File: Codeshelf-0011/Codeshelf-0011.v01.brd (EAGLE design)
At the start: 35 x 30 mm, 8 parts, among them SW1 A1202UA, U1 V_REG_LDOSMD, U2 MIC94061C6

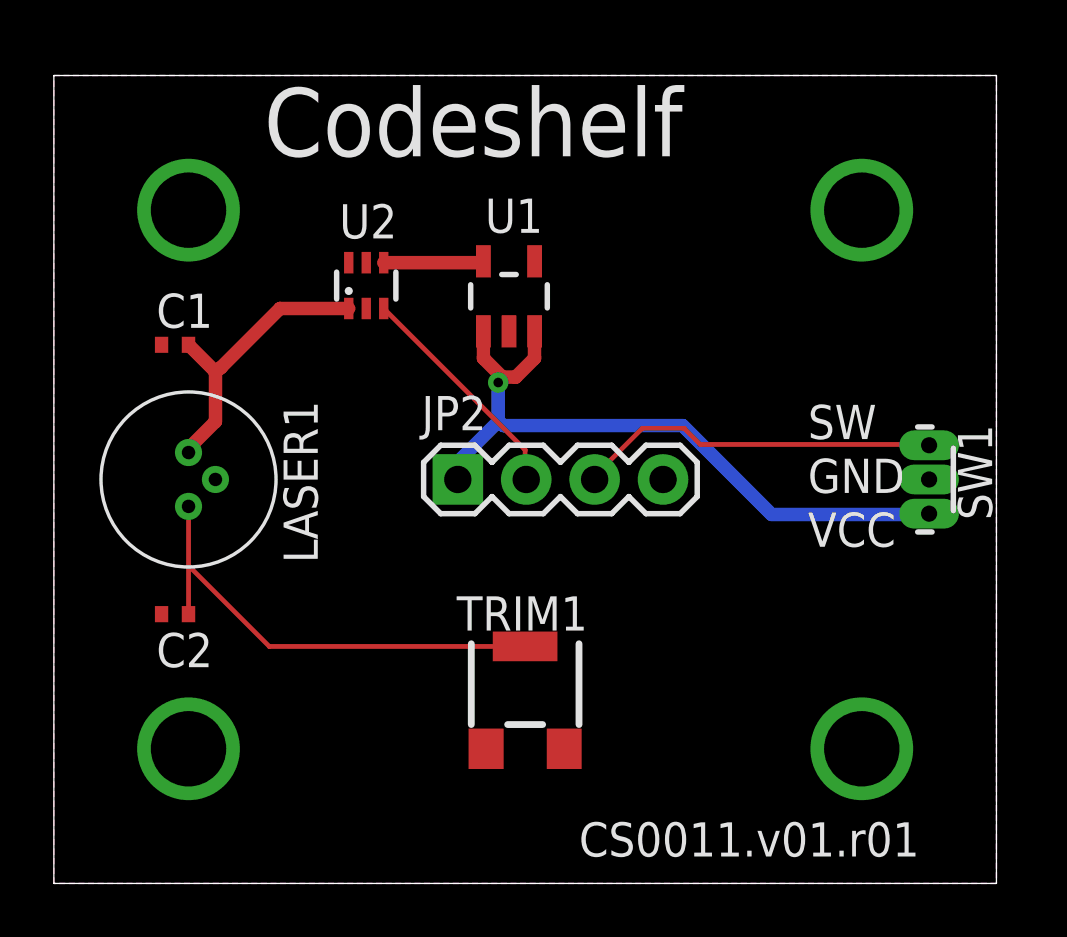
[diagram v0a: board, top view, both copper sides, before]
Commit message: cleanup repo
Cleaned up repo.
Cleaned up GW-devices.lbr
Add CS0012 - gateway dongle
CS0011 board changed to match laser from Laser66.
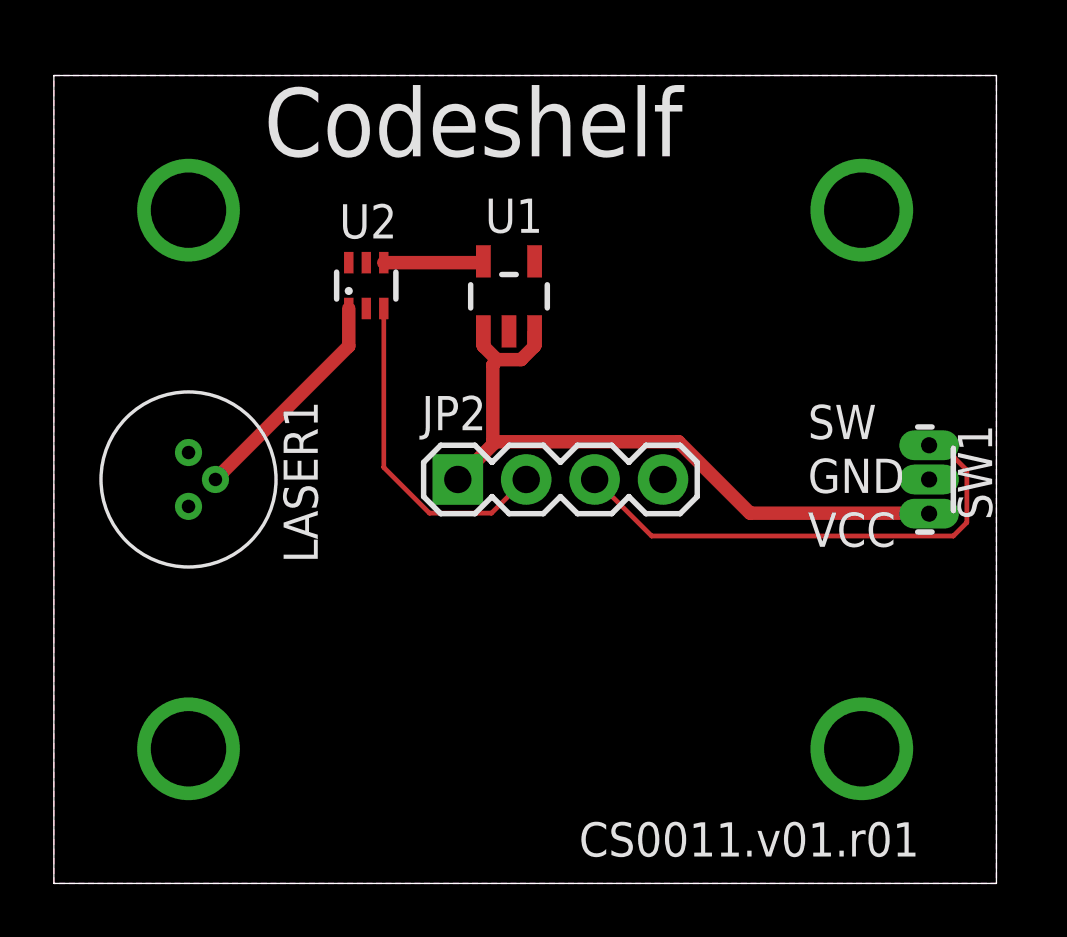
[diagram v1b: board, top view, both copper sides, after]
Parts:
- removed C1, C2: 0.1uF, GW-devices:C0402
- removed TRIM1: R-TRIM3364, GW-devices:RTRIM3364
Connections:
- removed net N$1: C1.1, LASER1.1, U2.1
- removed net N$4: C2.1, LASER1.3, TRIM1.2
- new net VCC: LASER1.2, U2.1
- net GND: now also LASER1.1; no longer C1.2, C2.2, LASER1.2, TRIM1.3
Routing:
- net N$4: track 17.7 -> 0.00 mm
- net N$1: track 10.7 -> 0.00 mm
- net VCC: track 0.00 -> 8.40 mm
- net N$3: track 13.6 -> 18.6 mm
- net N$2: track 8.56 -> 12.4 mm
- net +3V3: track 26.4 -> 25.8 mm, vias 1 -> 0
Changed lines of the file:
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@@
 <attribute name="NAME" x="16.011" y="24.159" size="1.27" layer="25"/>
 <attribute name="MFGN" value="Diodes Ince" x="16.9" y="21.8" size="1.778" layer="27" display="off"/>
-<attribute name="MFGP" value="AP7331-30WG-7" x="16.9" y="21.8" size="1.778" layer="27" display="off"/>
+<attribute name="MFGP" value="AP7331-28WG-7" x="16.9" y="21.8" size="1.778" layer="27" display="off"/>
 <attribute name="PRICE" value="0.50" x="16.9" y="21.8" size="1.778" layer="27" display="off"/>
-</element>
-<element name="TRIM1" library="GW-devices" package="RTRIM3364" value="R-TRIM3364" x="17.5" y="7" smashed="yes">
-<attribute name="NAME" x="14.96" y="9.39" size="1.27" layer="25"/>
-<attribute name="MFGN" value="Bourns" x="17.5" y="7" size="1.778" layer="27" display="off"/>
-<attribute name="MFGP" value="3364X-1-503E" x="17.5" y="7" size="1.778" layer="27" display="off"/>
-<attribute name="PRICE" value="1.00" x="17.5" y="7" size="1.778" layer="27" display="off"/>
-</element>
-<element name="C1" library="GW-devices" package="C0402" value="0.1uF" x="4.5" y="20" smashed="yes" rot="R180">
-<attribute name="NAME" x="5.9" y="21.9" size="1.27" layer="25" rot="R180"/>
-<attribute name="MFGN" value="Murata" x="4.5" y="20" size="1.778" layer="27" rot="R180" display="off"/>
-<attribute name="MFGP" value="GRM155R71C104JA88D" x="4.5" y="20" size="1.778" layer="27" rot="R180" display="off"/>
-<attribute name="PRICE" value="0.03" x="4.5" y="20" size="1.778" layer="27" rot="R180" display="off"/>
-</element>
-<element name="C2" library="GW-devices" package="C0402" value="0.1uF" x="4.5" y="10" smashed="yes" rot="R180">
-<attribute name="NAME" x="5.9" y="9.3" size="1.27" layer="25" rot="R180"/>
-<attribute name="MFGN" value="Murata" x="4.5" y="10" size="1.778" layer="27" rot="R180" display="off"/>
-<attribute name="MFGP" value="GRM155R71C104JA88D" x="4.5" y="10" size="1.778" layer="27" rot="R180" display="off"/>
-<attribute name="PRICE" value="0.03" x="4.5" y="10" size="1.778" layer="27" rot="R180" display="off"/>
 </element>
 </elements>
@@
 <contactref element="U2" pad="5"/>
 <contactref element="U2" pad="2"/>
-<contactref element="LASER1" pad="2"/>
 <contactref element="U1" pad="2"/>
 <contactref element="JP2" pad="4"/>
-<contactref element="TRIM1" pad="3"/>
-<contactref element="C2" pad="2"/>
-<contactref element="C1" pad="2"/>
 <polygon width="0.3048" layer="16">
 <vertex x="0" y="0"/>
@@
 <vertex x="35" y="0"/>
 </polygon>
+<contactref element="LASER1" pad="1"/>
 </signal>
 <signal name="+3V3" class="1">
@@
 <contactref element="U1" pad="3"/>
 <contactref element="JP2" pad="1"/>
-<wire x1="16.65" y1="18.8" x2="15.95" y2="19.5" width="0.5" layer="1"/>
-<wire x1="16.65" y1="18.8" x2="17.15" y2="18.8" width="0.5" layer="1"/>
-<wire x1="17.15" y1="18.8" x2="17.85" y2="19.5" width="0.5" layer="1"/>
-<wire x1="15.95" y1="19.5" x2="15.95" y2="20.4999" width="0.5" layer="1"/>
-<wire x1="17.85" y1="19.5" x2="17.85" y2="20.4999" width="0.5" layer="1"/>
-<wire x1="16.5" y1="17.15" x2="16.5" y2="18.6" width="0.5" layer="16"/>
-<wire x1="15" y1="15.65" x2="16.5" y2="17.15" width="0.5" layer="16"/>
-<wire x1="15" y1="15" x2="15" y2="15.65" width="0.5" layer="16"/>
-<wire x1="16.5" y1="18.6" x2="16.65" y2="18.8" width="0.5" layer="1"/>
-<wire x1="26.65" y1="13.7" x2="32.5" y2="13.7" width="0.5" layer="16"/>
-<wire x1="23.35" y1="17" x2="26.65" y2="13.7" width="0.5" layer="16"/>
-<wire x1="16.7" y1="17" x2="23.35" y2="17" width="0.5" layer="16"/>
-<wire x1="32.5" y1="13.7" x2="32.5" y2="13.73" width="0.5" layer="16"/>
-<wire x1="16.5" y1="17.15" x2="16.7" y2="17" width="0.5" layer="16"/>
-<via x="16.5" y="18.6" extent="1-16" drill="0.3556"/>
+<wire x1="15.95" y1="19.95" x2="15.95" y2="20.4999" width="0.5" layer="1"/>
+<wire x1="16.45" y1="19.45" x2="15.95" y2="19.95" width="0.5" layer="1"/>
+<wire x1="17.35" y1="19.45" x2="16.45" y2="19.45" width="0.5" layer="1"/>
+<wire x1="17.85" y1="19.95" x2="17.35" y2="19.45" width="0.5" layer="1"/>
+<wire x1="17.85" y1="20.4999" x2="17.85" y2="19.95" width="0.5" layer="1"/>
+<wire x1="16.3" y1="16.3" x2="16.3" y2="16.4" width="0.5" layer="1"/>
+<wire x1="16.3" y1="16.4" x2="16.3" y2="19.25" width="0.5" layer="1"/>
+<wire x1="15" y1="15" x2="16.3" y2="16.3" width="0.5" layer="1"/>
+<wire x1="16.3" y1="19.25" x2="16.45" y2="19.45" width="0.5" layer="1"/>
+<wire x1="25.85" y1="13.75" x2="32.5" y2="13.75" width="0.5" layer="1"/>
+<wire x1="23.2" y1="16.4" x2="25.85" y2="13.75" width="0.5" layer="1"/>
+<wire x1="16.3" y1="16.4" x2="23.2" y2="16.4" width="0.5" layer="1"/>
+<wire x1="32.5" y1="13.75" x2="32.5" y2="13.73" width="0.5" layer="1"/>
 </signal>
 <signal name="N$5">
@@
 <contactref element="U2" pad="4"/>
 <contactref element="U1" pad="5"/>
-<wire x1="12.25" y1="23.05" x2="15.9" y2="23.05" width="0.5" layer="1"/>
-<wire x1="15.9" y1="23.05" x2="15.95" y2="23.1001" width="0.5" layer="1"/>
-<wire x1="15.95" y1="23.1001" x2="15.95" y2="23.1" width="0.5" layer="1"/>
-</signal>
-<signal name="N$1" class="3">
-<contactref element="U2" pad="1"/>
-<contactref element="LASER1" pad="1"/>
-<contactref element="C1" pad="1"/>
-<wire x1="6" y1="19" x2="5" y2="20" width="0.5" layer="1"/>
-<wire x1="6" y1="17.15" x2="6" y2="19" width="0.5" layer="1"/>
-<wire x1="5" y1="16.15" x2="6" y2="17.15" width="0.5" layer="1"/>
-<wire x1="5" y1="16" x2="5" y2="16.15" width="0.5" layer="1"/>
-<wire x1="8.4" y1="21.35" x2="10.95" y2="21.35" width="0.5" layer="1"/>
-<wire x1="6.2" y1="19.15" x2="8.4" y2="21.35" width="0.5" layer="1"/>
-<wire x1="6" y1="19" x2="6.2" y2="19.15" width="0.5" layer="1"/>
+<wire x1="15.9" y1="23.05" x2="12.25" y2="23.05" width="0.5" layer="1"/>
+<wire x1="15.95" y1="23.1" x2="15.9" y2="23.05" width="0.5" layer="1"/>
+<wire x1="15.95" y1="23.1" x2="15.95" y2="23.1001" width="0.5" layer="1"/>
 </signal>
 <signal name="N$2">
 <contactref element="U2" pad="3"/>
 <contactref element="JP2" pad="2"/>
-<wire x1="17.5" y1="16.1" x2="12.25" y2="21.35" width="0.1778" layer="1"/>
-<wire x1="17.5" y1="15" x2="17.5" y2="16.1" width="0.1778" layer="1"/>
-<wire x1="17.54" y1="15" x2="17.5" y2="15" width="0.1778" layer="1"/>
+<wire x1="12.25" y1="15.45" x2="12.25" y2="21.35" width="0.1778" layer="1"/>
+<wire x1="13.95" y1="13.75" x2="12.25" y2="15.45" width="0.1778" layer="1"/>
+<wire x1="16.25" y1="13.75" x2="13.95" y2="13.75" width="0.1778" layer="1"/>
+<wire x1="17.5" y1="15" x2="16.25" y2="13.75" width="0.1778" layer="1"/>
+<wire x1="17.5" y1="15" x2="17.54" y2="15" width="0.1778" layer="1"/>
 </signal>
 <signal name="N$3">
 <contactref element="SW1" pad="3"/>
 <contactref element="JP2" pad="3"/>
-<wire x1="24" y1="16.3" x2="32.5" y2="16.3" width="0.1778" layer="1"/>
-<wire x1="23.4" y1="16.9" x2="24" y2="16.3" width="0.1778" layer="1"/>
-<wire x1="21.85" y1="16.9" x2="23.4" y2="16.9" width="0.1778" layer="1"/>
-<wire x1="20.1" y1="15.15" x2="21.85" y2="16.9" width="0.1778" layer="1"/>
-<wire x1="20.1" y1="15" x2="20.1" y2="15.15" width="0.1778" layer="1"/>
-<wire x1="32.5" y1="16.3" x2="32.5" y2="16.27" width="0.1778" layer="1"/>
-<wire x1="20.08" y1="15" x2="20.1" y2="15" width="0.1778" layer="1"/>
+<wire x1="33" y1="16.25" x2="32.5" y2="16.25" width="0.1778" layer="1"/>
+<wire x1="33.9" y1="15.35" x2="33" y2="16.25" width="0.1778" layer="1"/>
+<wire x1="33.9" y1="13.4" x2="33.9" y2="15.35" width="0.1778" layer="1"/>
+<wire x1="33.4" y1="12.9" x2="33.9" y2="13.4" width="0.1778" layer="1"/>
+<wire x1="22.2" y1="12.9" x2="33.4" y2="12.9" width="0.1778" layer="1"/>
+<wire x1="20.1" y1="15" x2="22.2" y2="12.9" width="0.1778" layer="1"/>
+<wire x1="32.5" y1="16.25" x2="32.5" y2="16.27" width="0.1778" layer="1"/>
+<wire x1="20.1" y1="15" x2="20.08" y2="15" width="0.1778" layer="1"/>
 </signal>
-<signal name="N$4">
-<contactref element="LASER1" pad="3"/>
-<contactref element="TRIM1" pad="2"/>
-<contactref element="C2" pad="1"/>
-<wire x1="5" y1="11.75" x2="5" y2="14" width="0.1778" layer="1"/>
-<wire x1="5" y1="10" x2="5" y2="11.75" width="0.1778" layer="1"/>
-<wire x1="8" y1="8.8" x2="17.5" y2="8.8" width="0.1778" layer="1"/>
-<wire x1="5.05" y1="11.75" x2="8" y2="8.8" width="0.1778" layer="1"/>
-<wire x1="5" y1="11.75" x2="5.05" y2="11.75" width="0.1778" layer="1"/>
+<signal name="VCC" class="3">
+<contactref element="U2" pad="1"/>
+<contactref element="LASER1" pad="2"/>
+<wire x1="10.95" y1="19.95" x2="10.95" y2="21.35" width="0.5" layer="1"/>
+<wire x1="6" y1="15" x2="10.95" y2="19.95" width="0.5" layer="1"/>
 </signal>
 </signals>
